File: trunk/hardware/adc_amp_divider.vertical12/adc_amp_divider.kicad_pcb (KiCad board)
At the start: 2 copper layers, 52.8 x 76.2 mm, 121 parts, among them M200 CONN_1, M201 CONN_1, M202 CONN_1, P201 CONN_10X2, P202 CONN_3, P203 CONN_2, P204 CONN_1, P205 CONN_1, P206 CONN_3, P207 CONN_2, P208 CONN_6, P209 CONN_6, U201 LMV324IDR, U202 LMV324IDR, U203 LMV324IDR

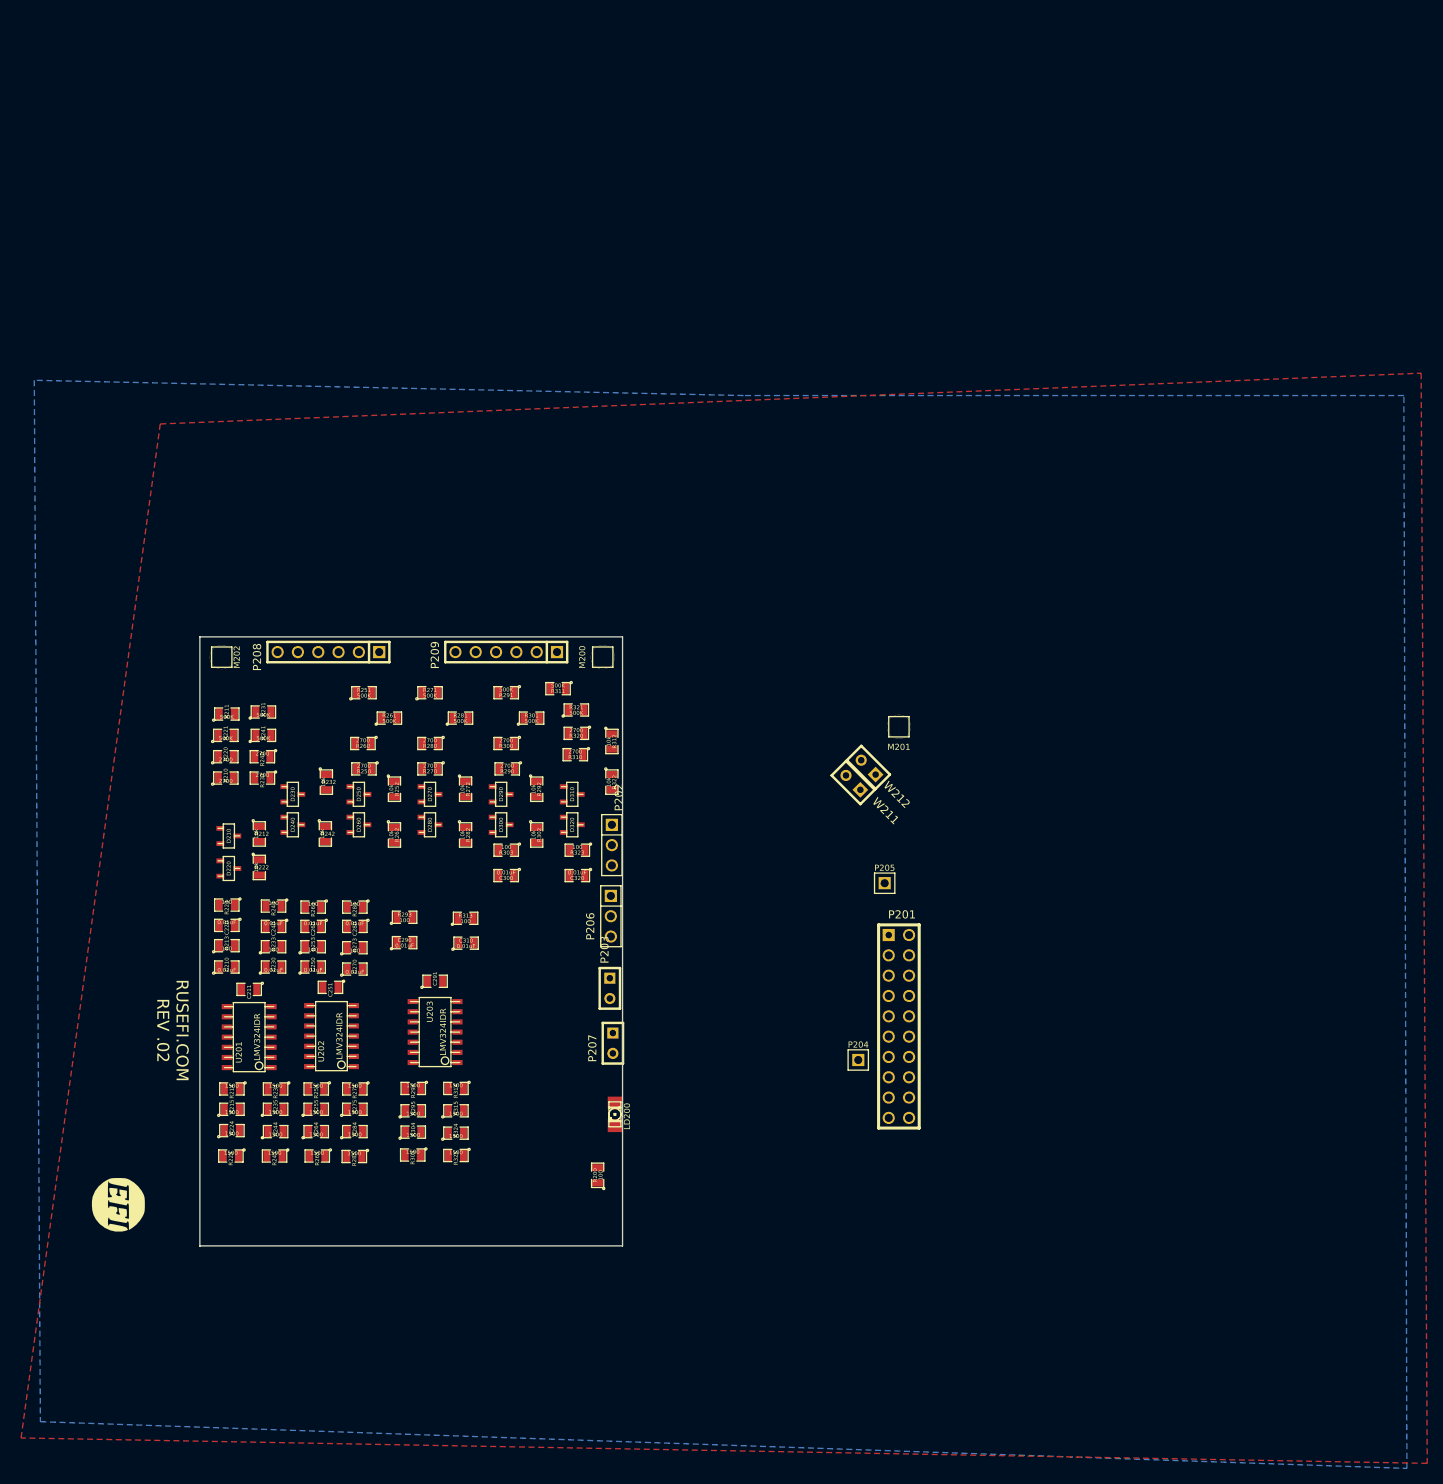
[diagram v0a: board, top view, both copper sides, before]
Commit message: 
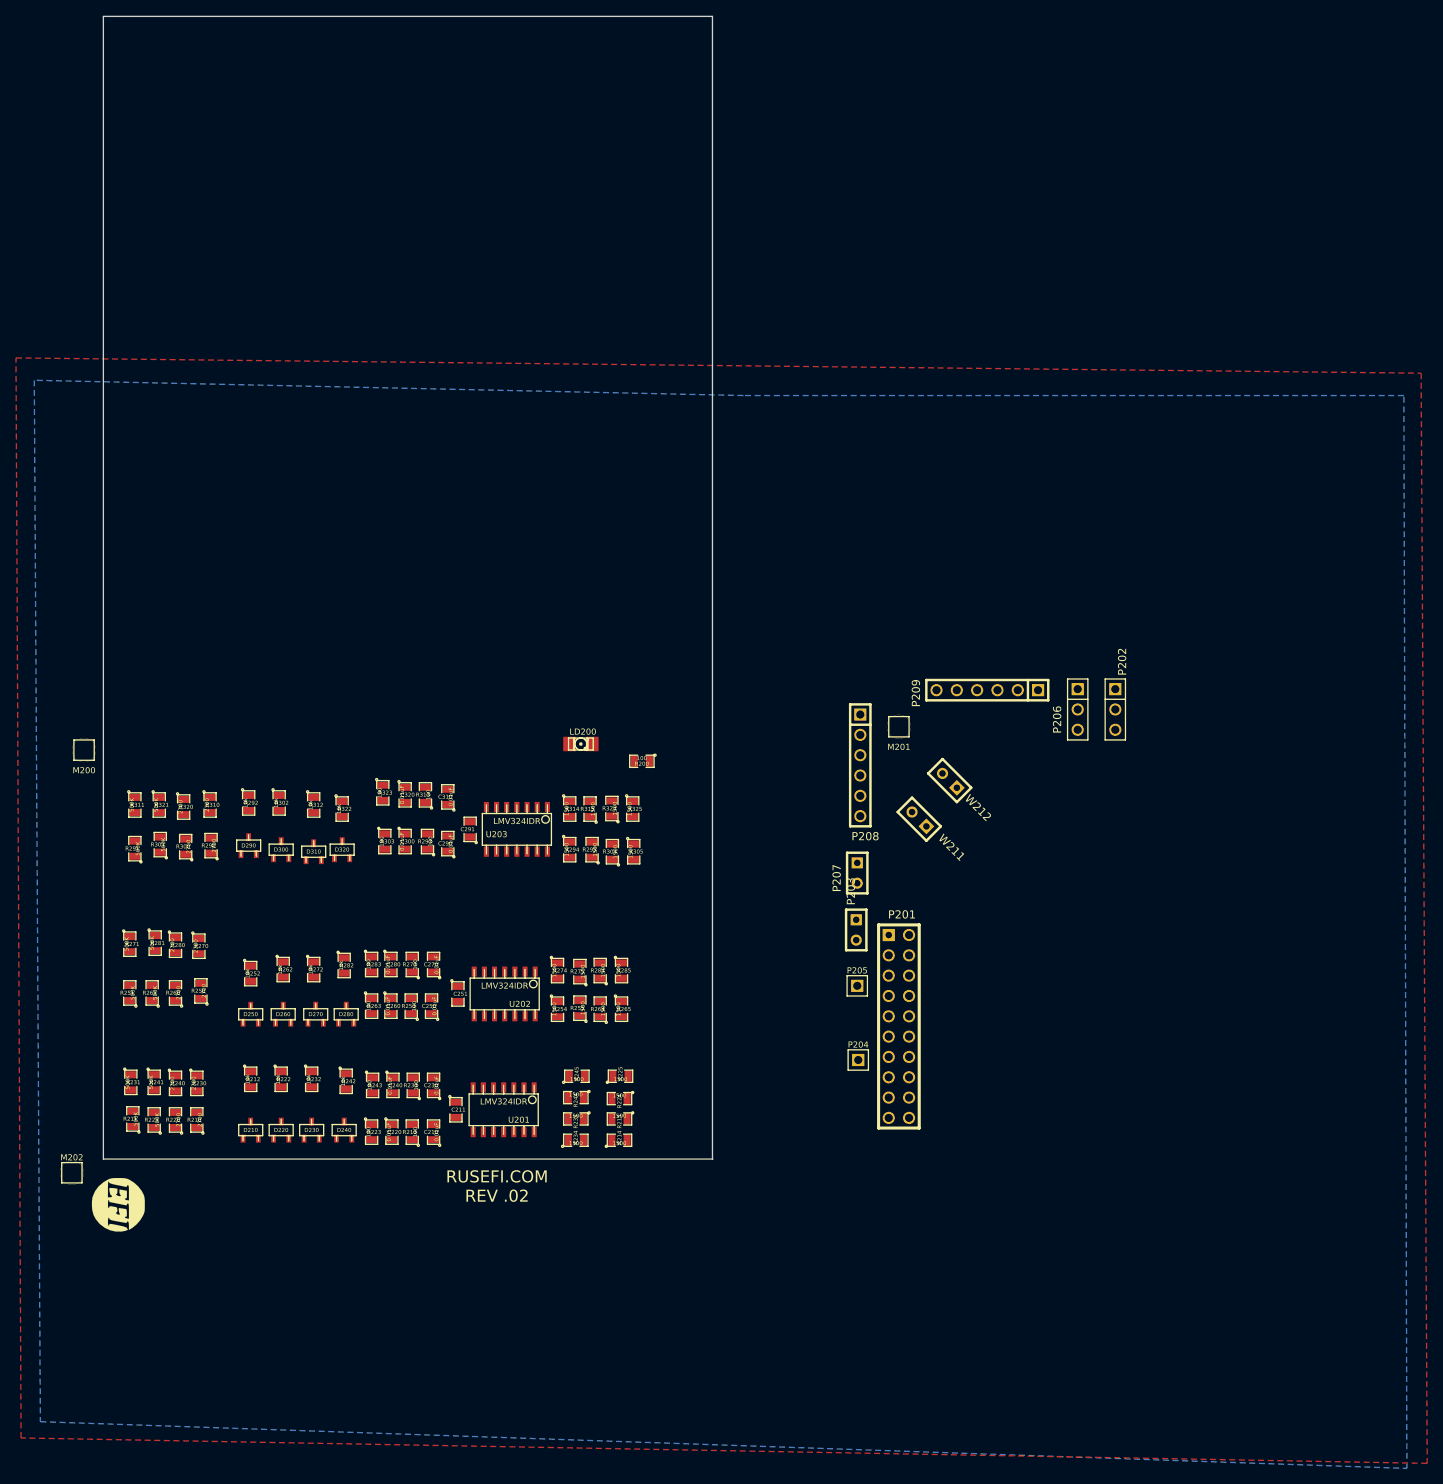
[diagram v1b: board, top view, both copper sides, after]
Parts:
- moved P208 68.0 mm to (123.4, 105.8), turned to 270 degrees
- moved M202 67.1 mm to (24.9, 156.7), turned to 0 degrees
- moved M200 65.9 mm to (26.4, 103.9), turned to 90 degrees
- moved P202 65.2 mm to (155.3, 98.8)
- moved P206 63.8 mm to (150.6, 98.8)
- moved P209 60.3 mm to (139.3, 96.4)
- moved R311 54.9 mm to (32.8, 110.7), turned to 270 degrees
- moved R321 53.5 mm to (35.8, 110.7), turned to 270 degrees
- moved R200 52.0 mm to (96.1, 105.3), turned to 180 degrees
- moved R211 52.0 mm to (32.5, 150.0), turned to 90 degrees
- moved R291 50.3 mm to (32.8, 116.2), turned to 90 degrees
- moved R320 49.9 mm to (38.9, 111.0), turned to 270 degrees
- moved R225 49.7 mm to (93.5, 144.7), turned to 0 degrees
- moved R231 49.2 mm to (32.3, 145.4), turned to 270 degrees
- moved R301 49.0 mm to (35.9, 115.7), turned to 90 degrees
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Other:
- board size 52.8 x 76.2 mm -> 76.2 x 142.8 mm

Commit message: getting closer
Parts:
- moved M202 148.1 mm to (171.7, 137.2)
- moved R291 126.9 mm to (159.3, 105.9)
- moved R311 126.8 mm to (159.3, 101.6)
- moved R321 126.8 mm to (162.3, 101.6)
- moved R301 126.7 mm to (162.3, 105.9)
- moved R320 126.6 mm to (165.1, 101.6)
- moved R300 126.4 mm to (165.1, 105.9)
- moved R310 126.3 mm to (168.1, 101.6)
- moved R290 126.1 mm to (168.0, 105.9)
- moved R292 118.6 mm to (165.6, 111.5), turned to 180 degrees
- moved R280 116.6 mm to (151.3, 101.2)
- moved R251 116.6 mm to (145.3, 106.2)
- moved R261 116.6 mm to (148.1, 106.2)
- moved R260 116.6 mm to (151.0, 106.2)
- moved R271 116.3 mm to (145.3, 101.1)
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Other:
- board size 76.2 x 142.8 mm -> 176.2 x 242.8 mm

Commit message: getting closer
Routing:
- net GND: track 0.00 -> 85.5 mm, vias 0 -> 47
- net /INP12: track 0.00 -> 71.8 mm, vias 0 -> 1
- net /OUT10: track 0.00 -> 68.5 mm
- net N-0000035: track 0.00 -> 63.9 mm
- net /OUT6: track 0.00 -> 62.9 mm
- net N-0000034: track 0.00 -> 60.9 mm
- net /INP7: track 0.00 -> 56.8 mm, vias 0 -> 1
- net /OUT11: track 0.00 -> 55.8 mm
- net /OUT12: track 0.00 -> 52.8 mm
- net /OUT7: track 0.00 -> 51.2 mm
- net /INP11: track 0.00 -> 48.3 mm, vias 0 -> 2
- net /INP4: track 0.00 -> 46.2 mm
- net /INP6: track 0.00 -> 45.6 mm, vias 0 -> 1
- net /INP8: track 0.00 -> 45.0 mm, vias 0 -> 1
- net /INP10: track 0.00 -> 45.0 mm
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
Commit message: DRC issues fixed
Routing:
- net VCC: track 0.00 -> 246.6 mm, vias 0 -> 9
- net GND: track 85.5 -> 54.8 mm, vias 47 -> 15
- net /OUT7: track 51.2 -> 23.4 mm, vias 0 -> 1
- net /INP12: track 71.8 -> 49.3 mm, vias 1 -> 2
- net /INP10: track 45.0 -> 66.2 mm, vias 0 -> 2
- net /OUT6: track 62.9 -> 45.4 mm
- net N-0000065: track 34.4 -> 18.8 mm
- net /OUT10: track 68.5 -> 53.9 mm, vias 0 -> 2
- net /INP7: track 56.8 -> 43.3 mm, vias 1 -> 2
- net /OUT11: track 55.8 -> 68.6 mm
- net N-0000054: track 33.7 -> 25.6 mm, vias 0 -> 2
- net N-0000046: track 21.0 -> 28.0 mm
- net /INP2: track 31.6 -> 24.5 mm, vias 0 -> 1
- net /OUT12: track 52.8 -> 58.8 mm
- net N-0000024: track 17.5 -> 23.1 mm
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- added copper zone on F.Cu, net GND
- removed copper zone on F.Cu, net VCC
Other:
- board size 176.2 x 242.8 mm -> 66 x 97.2 mm

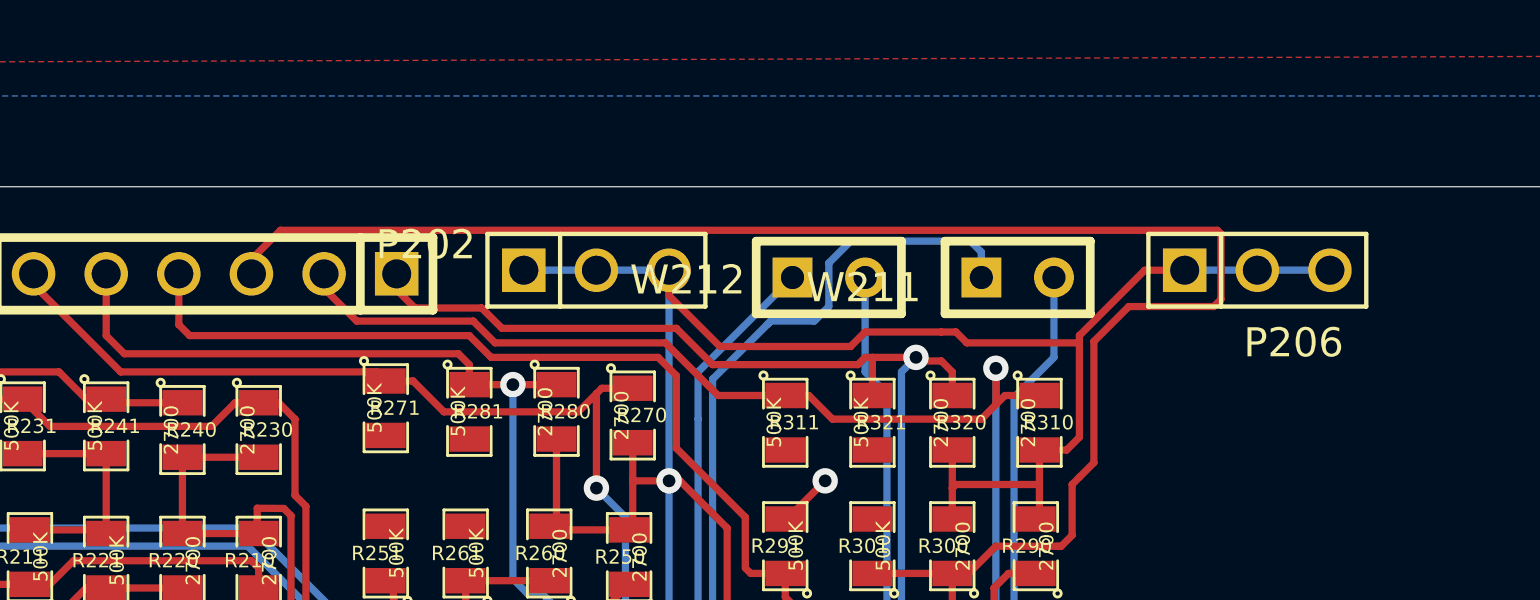
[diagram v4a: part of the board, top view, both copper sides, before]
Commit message: unneeded connector
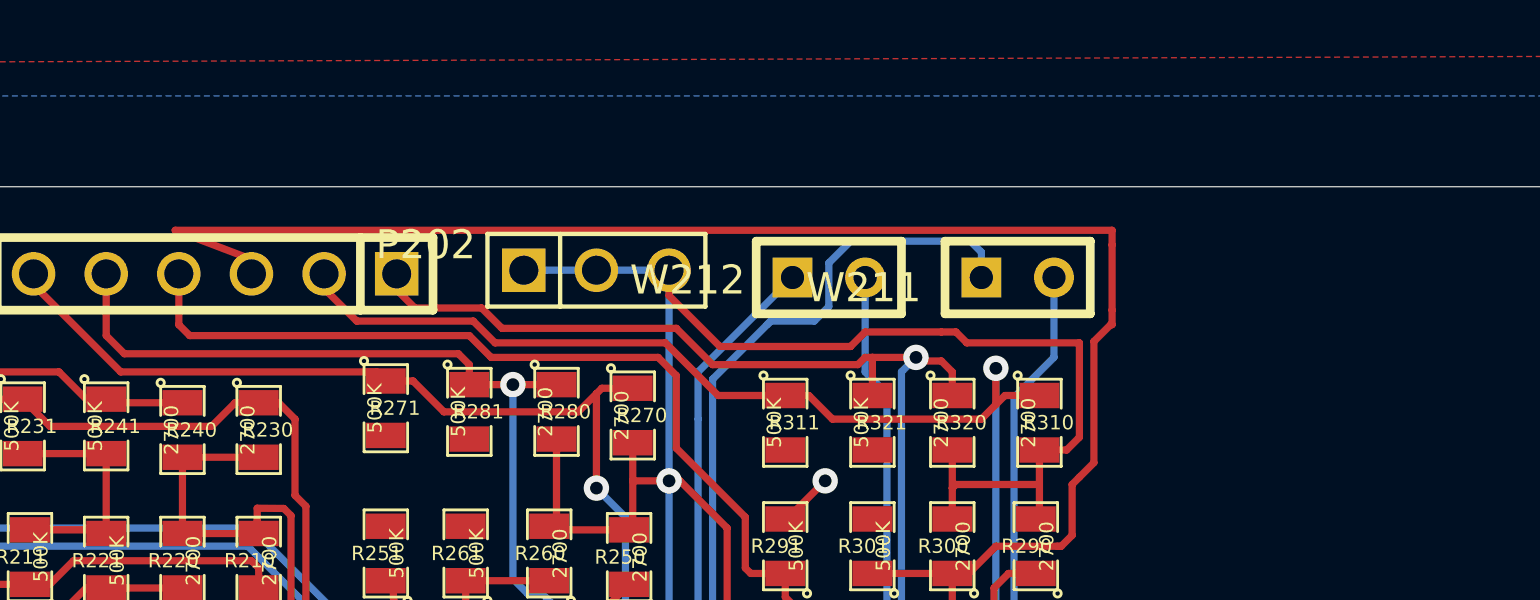
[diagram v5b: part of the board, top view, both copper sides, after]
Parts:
- removed P206: CONN_3, PIN_ARRAY_3X1
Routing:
- net VCC: track 246.6 -> 236.6 mm
- net /INP10: track 66.2 -> 64.2 mm

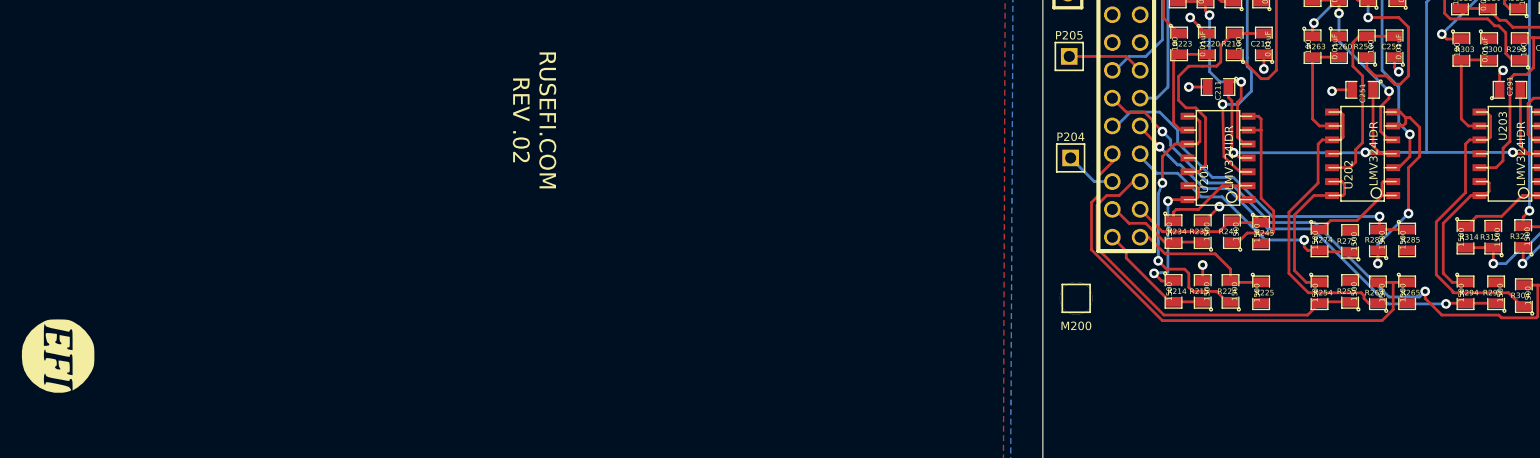
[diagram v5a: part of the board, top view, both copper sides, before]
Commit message: vcc > 5V
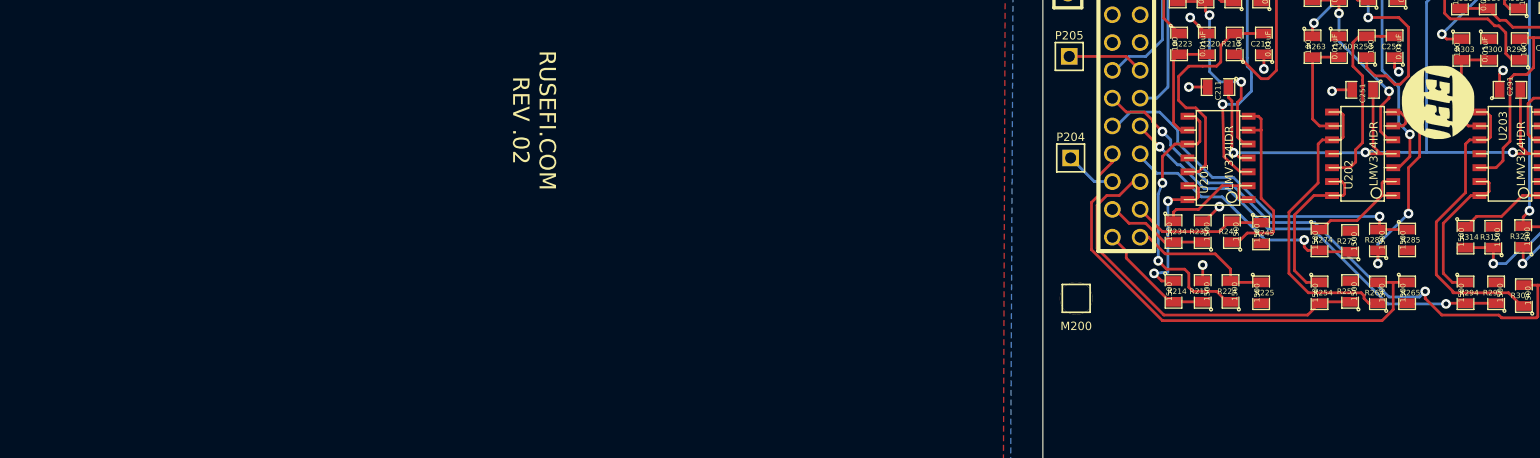
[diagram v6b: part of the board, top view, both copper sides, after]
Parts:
- moved G200 128.2 mm to (156.7, 137.5)
- moved G201 82.0 mm to (143.1, 139.2)
- moved G202 58.4 mm to (172.1, 113.7)
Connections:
- net VCC renamed /5V
